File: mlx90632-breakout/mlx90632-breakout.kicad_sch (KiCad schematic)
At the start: 8 parts, among them J1 Conn_01x04_Male, U1 MLX90632SLD-BCB-000-SP

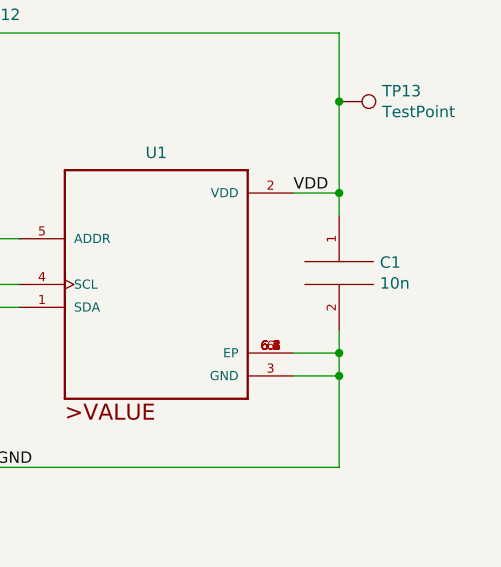
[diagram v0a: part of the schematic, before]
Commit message: updated breakout boards
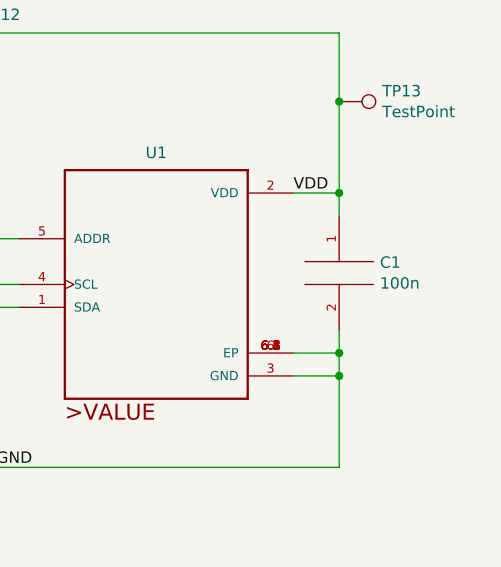
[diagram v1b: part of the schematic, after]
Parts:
- C1: value 10n -> 100n
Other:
- company: (none) -> Melexis Inc
- title: (none) -> mlx90632-breakout
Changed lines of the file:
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@@
 (kicad_sch (version 20211123) (generator eeschema)
   (paper "A3")
+  (title_block
+    (title "mlx90632-breakout")
+    (date "2023-01-16")
+    (rev "1.2")
+    (company "Melexis Inc")
+  )
   (junction (at 144.78 66.04) (diameter 0) (color 0 0 0 0)
   )
@@
       (effects (font (size 1.27 1.27)) (justify left))
     )
-    (property "Value" "10n" (id 1) (at 208.9912 65.913 0)
+    (property "Value" "100n" (id 1) (at 208.9912 65.913 0)
       (effects (font (size 1.27 1.27)) (justify left))
     )
@@
   (symbol_instances
     (path "/00000000-0000-0000-0000-00005ee38154"
-      (reference "C1") (unit 1) (value "10n") (footprint "Capacitor_SMD:C_0402_1005Metric")
+      (reference "C1") (unit 1) (value "100n") (footprint "Capacitor_SMD:C_0402_1005Metric")
     )
     (path "/020fb5f8-7154-449f-9427-c21c224740aa"
